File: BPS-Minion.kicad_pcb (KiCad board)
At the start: 2 copper layers, 85 x 66 mm, 128 parts, among them J1 TopConn, J10 TempConn2, J2 BottomConn, J3 DTENConfig, J4 IsoConfig, J5 IN, J6 OUT, J8 RegularSPIConn, J9 TempConn1, Q1 BSS308PE, Q10 BSS308PE, Q11 BSS308PE, Q12 BSS308PE, Q13 NSV1C201MZ4, Q2 BSS308PE, Q3 BSS308PE, Q4 BSS308PE, Q5 BSS308PE, Q6 BSS308PE, Q7 BSS308PE, Q8 BSS308PE, Q9 BSS308PE, SW1 Power Switch, U1 LTC6811-1, U2 HX1188FNL, U3 LTC6255, U4 LTC1380, U5 LTC1380

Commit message: Added measurements
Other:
- net class Default removed

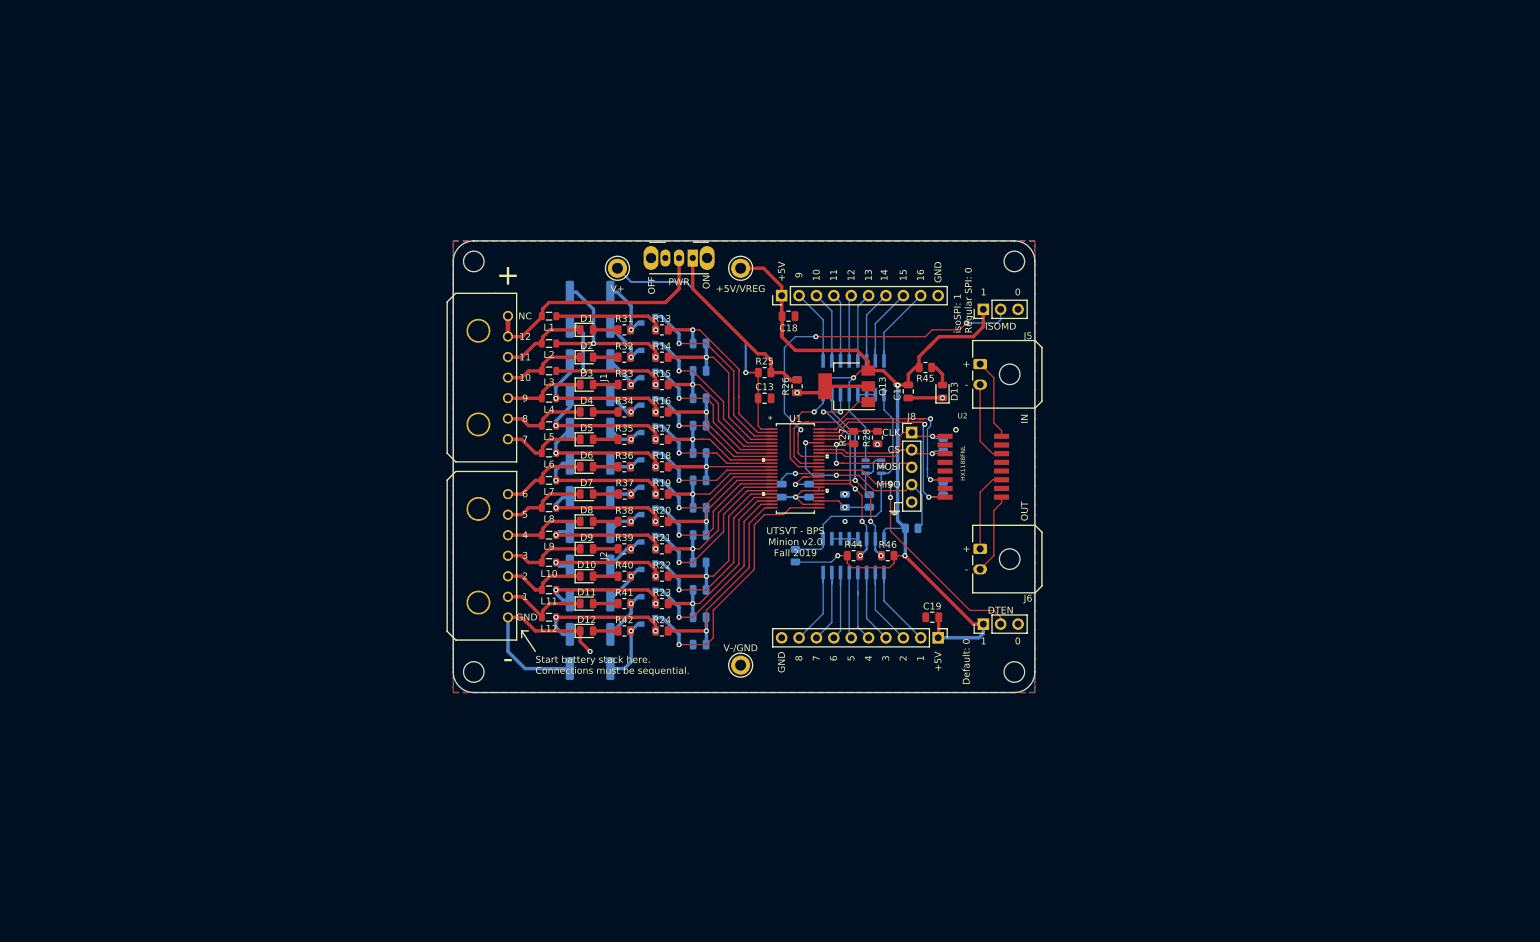
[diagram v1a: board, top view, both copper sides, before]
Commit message: define edge cuts for new volttemp
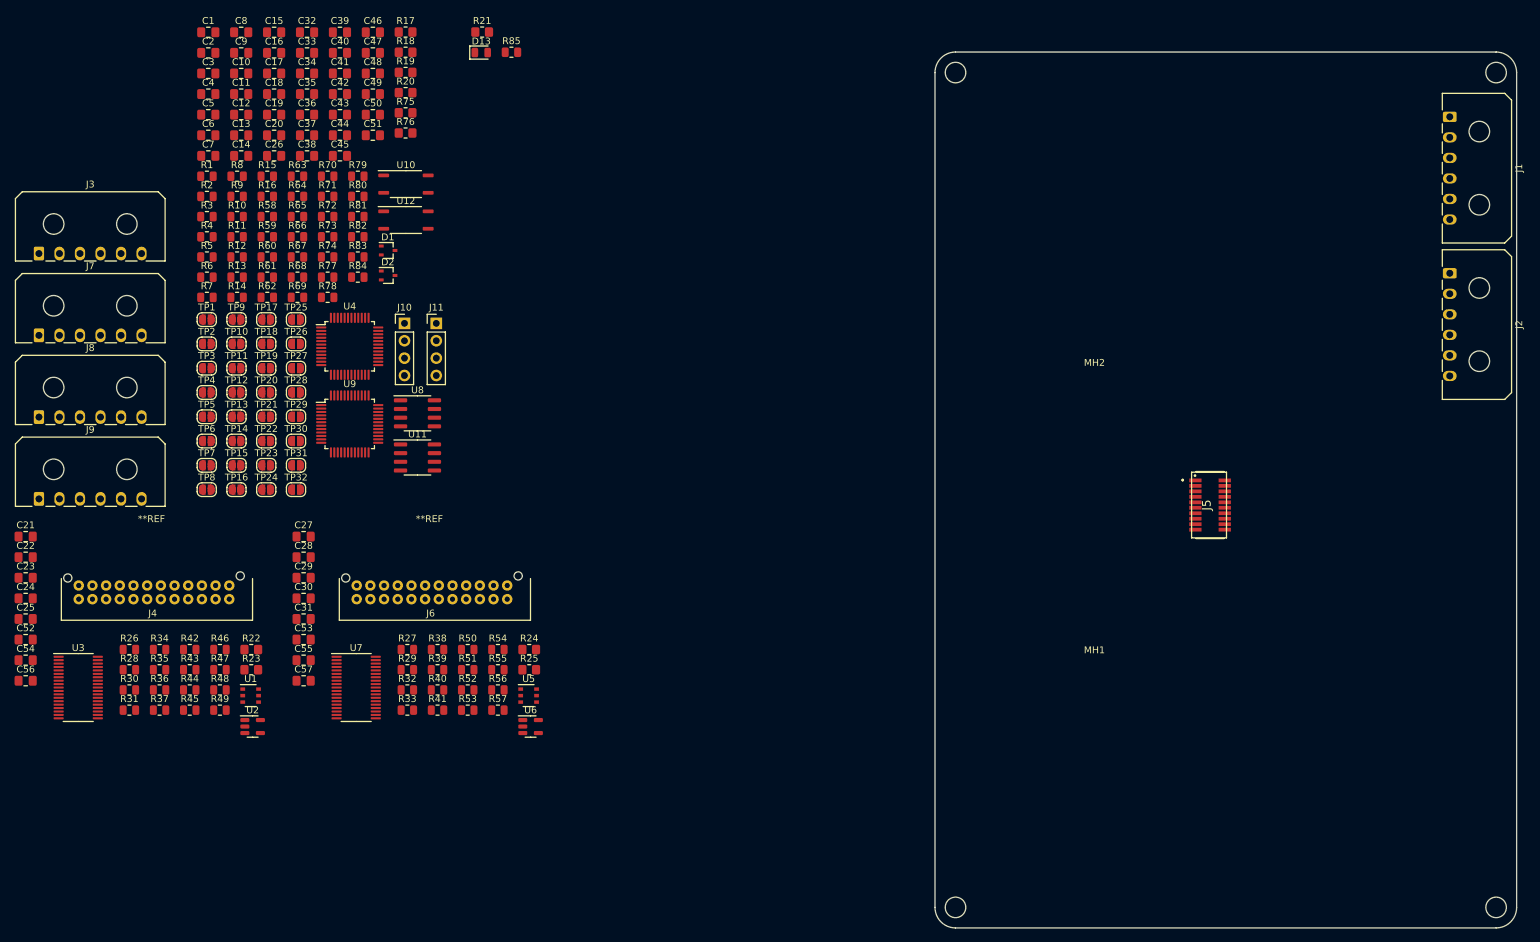
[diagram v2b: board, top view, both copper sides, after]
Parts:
- removed D10, D11, D12, D3, D4, D5, D6, D7, D8, D9: Red, LED_SMD:LED_0805_2012Metric
- removed L1, L10, L11, L12, L2, L3, L4, L5, L6, L7, L8, L9: 600, Inductor_SMD:L_0805_2012Metric
- removed Q1, Q10, Q11, Q12, Q2, Q3, Q4, Q5, Q6, Q7, Q8, Q9: BSS308PE, Package_TO_SOT_SMD:SOT-23
- removed Q13: NSV1C201MZ4, Package_TO_SOT_SMD:SOT-223
- removed SW1: Power Switch, Button_Switch_THT:SW_CuK_OS102011MA1QN1_SPDT_Angled
- added C21: 47n, Capacitor_SMD:C_0805_2012Metric_Pad1.18x1.45mm_HandSolder, F.Cu at (32.5, 93.2)
- added C22: 47n, Capacitor_SMD:C_0805_2012Metric_Pad1.18x1.45mm_HandSolder, F.Cu at (32.5, 96.2)
- added C23: 4.7u, Capacitor_SMD:C_0805_2012Metric_Pad1.18x1.45mm_HandSolder, F.Cu at (32.5, 99.2)
- added C24: 1u, Capacitor_SMD:C_0805_2012Metric_Pad1.18x1.45mm_HandSolder, F.Cu at (32.5, 102.2)
- added C25: 10u, Capacitor_SMD:C_0805_2012Metric_Pad1.18x1.45mm_HandSolder, F.Cu at (32.5, 105.2)
- added C26: 1u, Capacitor_SMD:C_0805_2012Metric_Pad1.18x1.45mm_HandSolder, F.Cu at (68.8, 37.6)
- added C27: 47n, Capacitor_SMD:C_0805_2012Metric_Pad1.18x1.45mm_HandSolder, F.Cu at (73.1, 93.2)
- added C28: 47n, Capacitor_SMD:C_0805_2012Metric_Pad1.18x1.45mm_HandSolder, F.Cu at (73.1, 96.2)
- added C29: 4.7u, Capacitor_SMD:C_0805_2012Metric_Pad1.18x1.45mm_HandSolder, F.Cu at (73.1, 99.2)
- added C30: 1u, Capacitor_SMD:C_0805_2012Metric_Pad1.18x1.45mm_HandSolder, F.Cu at (73.1, 102.2)
- added C31: 10u, Capacitor_SMD:C_0805_2012Metric_Pad1.18x1.45mm_HandSolder, F.Cu at (73.1, 105.2)
- added C32: 220nF, Capacitor_SMD:C_0805_2012Metric_Pad1.18x1.45mm_HandSolder, F.Cu at (73.6, 19.5)
- added C33: 220nF, Capacitor_SMD:C_0805_2012Metric_Pad1.18x1.45mm_HandSolder, F.Cu at (73.6, 22.5)
- added C34: 220nF, Capacitor_SMD:C_0805_2012Metric_Pad1.18x1.45mm_HandSolder, F.Cu at (73.6, 25.5)
- added C35: 220nF, Capacitor_SMD:C_0805_2012Metric_Pad1.18x1.45mm_HandSolder, F.Cu at (73.6, 28.5)
- added C36: 220nF, Capacitor_SMD:C_0805_2012Metric_Pad1.18x1.45mm_HandSolder, F.Cu at (73.6, 31.6)
- added C37: 220nF, Capacitor_SMD:C_0805_2012Metric_Pad1.18x1.45mm_HandSolder, F.Cu at (73.6, 34.6)
- added C38: 220nF, Capacitor_SMD:C_0805_2012Metric_Pad1.18x1.45mm_HandSolder, F.Cu at (73.6, 37.6)
- added C39: 220nF, Capacitor_SMD:C_0805_2012Metric_Pad1.18x1.45mm_HandSolder, F.Cu at (78.4, 19.5)
- added C40: 220nF, Capacitor_SMD:C_0805_2012Metric_Pad1.18x1.45mm_HandSolder, F.Cu at (78.4, 22.5)
- added C41: 220nF, Capacitor_SMD:C_0805_2012Metric_Pad1.18x1.45mm_HandSolder, F.Cu at (78.4, 25.5)
- added C42: 220nF, Capacitor_SMD:C_0805_2012Metric_Pad1.18x1.45mm_HandSolder, F.Cu at (78.4, 28.5)
- added C43: 220nF, Capacitor_SMD:C_0805_2012Metric_Pad1.18x1.45mm_HandSolder, F.Cu at (78.4, 31.6)
- added C44: 220nF, Capacitor_SMD:C_0805_2012Metric_Pad1.18x1.45mm_HandSolder, F.Cu at (78.4, 34.6)
- added C45: 220nF, Capacitor_SMD:C_0805_2012Metric_Pad1.18x1.45mm_HandSolder, F.Cu at (78.4, 37.6)
- added C46: 220nF, Capacitor_SMD:C_0805_2012Metric_Pad1.18x1.45mm_HandSolder, F.Cu at (83.3, 19.5)
- added C47: 220nF, Capacitor_SMD:C_0805_2012Metric_Pad1.18x1.45mm_HandSolder, F.Cu at (83.3, 22.5)
- added C48: .47u, Capacitor_SMD:C_0805_2012Metric_Pad1.18x1.45mm_HandSolder, F.Cu at (83.3, 25.5)
- added C49: 100p, Capacitor_SMD:C_0805_2012Metric_Pad1.18x1.45mm_HandSolder, F.Cu at (83.3, 28.5)
- added C50: 220nF, Capacitor_SMD:C_0805_2012Metric_Pad1.18x1.45mm_HandSolder, F.Cu at (83.3, 31.6)
- added C51: 1u, Capacitor_SMD:C_0805_2012Metric_Pad1.18x1.45mm_HandSolder, F.Cu at (83.3, 34.6)
- added C52: 1u, Capacitor_SMD:C_0805_2012Metric_Pad1.18x1.45mm_HandSolder, F.Cu at (32.5, 108.3)
- added C53: 1u, Capacitor_SMD:C_0805_2012Metric_Pad1.18x1.45mm_HandSolder, F.Cu at (73.1, 108.3)
- added C54: 1u, Capacitor_SMD:C_0805_2012Metric_Pad1.18x1.45mm_HandSolder, F.Cu at (32.5, 111.3)
- added C55: 1u, Capacitor_SMD:C_0805_2012Metric_Pad1.18x1.45mm_HandSolder, F.Cu at (73.1, 111.3)
- added C56: 1u, Capacitor_SMD:C_0805_2012Metric_Pad1.18x1.45mm_HandSolder, F.Cu at (32.5, 114.3)
- added C57: 1u, Capacitor_SMD:C_0805_2012Metric_Pad1.18x1.45mm_HandSolder, F.Cu at (73.1, 114.3)
- added J11: BMS2OTP, Connector_PinHeader_2.54mm:PinHeader_1x04_P2.54mm_Vertical, F.Cu at (92.5, 62.0)
- added J7: TopConn, Connector_Molex:Molex_Micro-Fit_3.0_43650-0600_1x06_P3.00mm_Horizontal, F.Cu at (34.5, 63.8)
- added R49: 10k, Resistor_SMD:R_0805_2012Metric, F.Cu at (60.9, 118.6)
- added R50: 10k, Resistor_SMD:R_0805_2012Metric, F.Cu at (97.1, 109.7)
- added R51: 10k, Resistor_SMD:R_0805_2012Metric, F.Cu at (97.1, 112.7)
- added R52: 10k, Resistor_SMD:R_0805_2012Metric, F.Cu at (97.1, 115.6)
- added R53: 10k, Resistor_SMD:R_0805_2012Metric, F.Cu at (97.1, 118.6)
- added R54: 10k, Resistor_SMD:R_0805_2012Metric, F.Cu at (101.5, 109.7)
- added R55: 10k, Resistor_SMD:R_0805_2012Metric, F.Cu at (101.5, 112.7)
- added R56: 10k, Resistor_SMD:R_0805_2012Metric, F.Cu at (101.5, 115.6)
- added R57: 10k, Resistor_SMD:R_0805_2012Metric, F.Cu at (101.5, 118.6)
- added R58: 20, Resistor_SMD:R_0805_2012Metric, F.Cu at (67.8, 46.5)
- added R59: 20, Resistor_SMD:R_0805_2012Metric, F.Cu at (67.8, 49.4)
- added R60: 20, Resistor_SMD:R_0805_2012Metric, F.Cu at (67.8, 52.4)
- added R61: 20, Resistor_SMD:R_0805_2012Metric, F.Cu at (67.8, 55.3)
- added R62: 20, Resistor_SMD:R_0805_2012Metric, F.Cu at (67.8, 58.2)
- added R63: 20, Resistor_SMD:R_0805_2012Metric, F.Cu at (72.2, 40.5)
- added R64: 20, Resistor_SMD:R_0805_2012Metric, F.Cu at (72.2, 43.5)
- added R65: 20, Resistor_SMD:R_0805_2012Metric, F.Cu at (72.2, 46.5)
- added R66: 20, Resistor_SMD:R_0805_2012Metric, F.Cu at (72.2, 49.4)
- added R67: 20, Resistor_SMD:R_0805_2012Metric, F.Cu at (72.2, 52.4)
- added R68: 20, Resistor_SMD:R_0805_2012Metric, F.Cu at (72.2, 55.3)
- added R69: 20, Resistor_SMD:R_0805_2012Metric, F.Cu at (72.2, 58.2)
- added R70: 20, Resistor_SMD:R_0805_2012Metric, F.Cu at (76.6, 40.5)
- added R71: 20, Resistor_SMD:R_0805_2012Metric, F.Cu at (76.6, 43.5)
- added R72: 20, Resistor_SMD:R_0805_2012Metric, F.Cu at (76.6, 46.5)
- added R73: 20, Resistor_SMD:R_0805_2012Metric, F.Cu at (76.6, 49.4)
- added R74: 20, Resistor_SMD:R_0805_2012Metric, F.Cu at (76.6, 52.4)
- added R75: 10k, Resistor_SMD:R_0805_2012Metric_Pad1.20x1.40mm_HandSolder, F.Cu at (88.0, 31.3)
- added R76: 100, Resistor_SMD:R_0805_2012Metric_Pad1.20x1.40mm_HandSolder, F.Cu at (88.0, 34.2)
- added R77: 10k, Resistor_SMD:R_0805_2012Metric, F.Cu at (76.6, 55.3)
- added R78: 10k, Resistor_SMD:R_0805_2012Metric, F.Cu at (76.6, 58.2)
- added R79: 220, Resistor_SMD:R_0805_2012Metric, F.Cu at (81.1, 40.5)
- added R80: 1k, Resistor_SMD:R_0805_2012Metric, F.Cu at (81.1, 43.5)
- added R81: 10k, Resistor_SMD:R_0805_2012Metric, F.Cu at (81.1, 46.5)
- added R82: 10k, Resistor_SMD:R_0805_2012Metric, F.Cu at (81.1, 49.4)
- added R83: 220, Resistor_SMD:R_0805_2012Metric, F.Cu at (81.1, 52.4)
- added R84: 10k, Resistor_SMD:R_0805_2012Metric, F.Cu at (81.1, 55.3)
- added R85: 50, Resistor_SMD:R_0805_2012Metric, F.Cu at (103.5, 22.4)
- added TP10: TestPoint_2Pole, Jumper:SolderJumper-2_P1.3mm_Open_RoundedPad1.0x1.5mm, F.Cu at (63.3, 65.0)
- added TP11: TestPoint_2Pole, Jumper:SolderJumper-2_P1.3mm_Open_RoundedPad1.0x1.5mm, F.Cu at (63.3, 68.6)
- added TP12: TestPoint_2Pole, Jumper:SolderJumper-2_P1.3mm_Open_RoundedPad1.0x1.5mm, F.Cu at (63.3, 72.2)
- added TP13: TestPoint_2Pole, Jumper:SolderJumper-2_P1.3mm_Open_RoundedPad1.0x1.5mm, F.Cu at (63.3, 75.7)
- added TP14: TestPoint_2Pole, Jumper:SolderJumper-2_P1.3mm_Open_RoundedPad1.0x1.5mm, F.Cu at (63.3, 79.2)
- added TP15: TestPoint_2Pole, Jumper:SolderJumper-2_P1.3mm_Open_RoundedPad1.0x1.5mm, F.Cu at (63.3, 82.8)
- added TP16: TestPoint_2Pole, Jumper:SolderJumper-2_P1.3mm_Open_RoundedPad1.0x1.5mm, F.Cu at (63.3, 86.3)
- added TP17: TestPoint_2Pole, Jumper:SolderJumper-2_P1.3mm_Open_RoundedPad1.0x1.5mm, F.Cu at (67.7, 61.5)
- added TP18: TestPoint_2Pole, Jumper:SolderJumper-2_P1.3mm_Open_RoundedPad1.0x1.5mm, F.Cu at (67.7, 65.0)
- added TP19: TestPoint_2Pole, Jumper:SolderJumper-2_P1.3mm_Open_RoundedPad1.0x1.5mm, F.Cu at (67.7, 68.6)
- added TP20: TestPoint_2Pole, Jumper:SolderJumper-2_P1.3mm_Open_RoundedPad1.0x1.5mm, F.Cu at (67.7, 72.2)
- added TP21: TestPoint_2Pole, Jumper:SolderJumper-2_P1.3mm_Open_RoundedPad1.0x1.5mm, F.Cu at (67.7, 75.7)
- added TP22: TestPoint_2Pole, Jumper:SolderJumper-2_P1.3mm_Open_RoundedPad1.0x1.5mm, F.Cu at (67.7, 79.2)
- added TP23: TestPoint_2Pole, Jumper:SolderJumper-2_P1.3mm_Open_RoundedPad1.0x1.5mm, F.Cu at (67.7, 82.8)
- added TP24: TestPoint_2Pole, Jumper:SolderJumper-2_P1.3mm_Open_RoundedPad1.0x1.5mm, F.Cu at (67.7, 86.3)
- added TP25: TestPoint_2Pole, Jumper:SolderJumper-2_P1.3mm_Open_RoundedPad1.0x1.5mm, F.Cu at (72.0, 61.5)
- added TP26: TestPoint_2Pole, Jumper:SolderJumper-2_P1.3mm_Open_RoundedPad1.0x1.5mm, F.Cu at (72.0, 65.0)
- added TP27: TestPoint_2Pole, Jumper:SolderJumper-2_P1.3mm_Open_RoundedPad1.0x1.5mm, F.Cu at (72.0, 68.6)
- added TP28: TestPoint_2Pole, Jumper:SolderJumper-2_P1.3mm_Open_RoundedPad1.0x1.5mm, F.Cu at (72.0, 72.2)
- added TP29: TestPoint_2Pole, Jumper:SolderJumper-2_P1.3mm_Open_RoundedPad1.0x1.5mm, F.Cu at (72.0, 75.7)
- added TP30: TestPoint_2Pole, Jumper:SolderJumper-2_P1.3mm_Open_RoundedPad1.0x1.5mm, F.Cu at (72.0, 79.2)
- added TP31: TestPoint_2Pole, Jumper:SolderJumper-2_P1.3mm_Open_RoundedPad1.0x1.5mm, F.Cu at (72.0, 82.8)
- added TP32: TestPoint_2Pole, Jumper:SolderJumper-2_P1.3mm_Open_RoundedPad1.0x1.5mm, F.Cu at (72.0, 86.3)
- added TP4: TestPoint_2Pole, Jumper:SolderJumper-2_P1.3mm_Open_RoundedPad1.0x1.5mm, F.Cu at (59.0, 72.2)
- added TP5: TestPoint_2Pole, Jumper:SolderJumper-2_P1.3mm_Open_RoundedPad1.0x1.5mm, F.Cu at (59.0, 75.7)
- added TP6: TestPoint_2Pole, Jumper:SolderJumper-2_P1.3mm_Open_RoundedPad1.0x1.5mm, F.Cu at (59.0, 79.2)
- added TP7: TestPoint_2Pole, Jumper:SolderJumper-2_P1.3mm_Open_RoundedPad1.0x1.5mm, F.Cu at (59.0, 82.8)
- added TP8: TestPoint_2Pole, Jumper:SolderJumper-2_P1.3mm_Open_RoundedPad1.0x1.5mm, F.Cu at (59.0, 86.3)
- added TP9: TestPoint_2Pole, Jumper:SolderJumper-2_P1.3mm_Open_RoundedPad1.0x1.5mm, F.Cu at (63.3, 61.5)
- added U10: TLP185, Package_SO:SOIC-4_4.55x3.7mm_P2.54mm, F.Cu at (88.1, 41.7)
- added U11: ISO1640BDR, Package_SO:SOIC-8_3.9x4.9mm_P1.27mm, F.Cu at (89.8, 81.7)
- added U12: TLP185, Package_SO:SOIC-4_4.55x3.7mm_P2.54mm, F.Cu at (88.1, 47.0)
- added U6: LM321, Package_TO_SOT_SMD:SOT-23-5, F.Cu at (106.3, 121.0)
- added U7: ADS7953SBDBT, Package_SO:TSSOP-38_4.4x9.7mm_P0.5mm, F.Cu at (80.8, 115.3)
- added U8: ISO1640BDR, Package_SO:SOIC-8_3.9x4.9mm_P1.27mm, F.Cu at (89.8, 75.2)
- added U9: BQ7695201PFBR, Package_QFP:TQFP-48_7x7mm_P0.5mm, F.Cu at (79.9, 76.8)
- C1, C10, C11, C12, C2, C3, C4, C5, C6, C7, C8, C9: value 10n -> 220nF; footprint Capacitor_SMD:C_0805_2012Metric -> Capacitor_SMD:C_0805_2012Metric_Pad1.18x1.45mm_HandSolder; moved to F.Cu
- C13: value 100n -> 220nF; footprint Capacitor_SMD:C_0805_2012Metric -> Capacitor_SMD:C_0805_2012Metric_Pad1.18x1.45mm_HandSolder
- C14, C15: value 1u -> 220nF; footprint Capacitor_SMD:C_0805_2012Metric -> Capacitor_SMD:C_0805_2012Metric_Pad1.18x1.45mm_HandSolder; moved to F.Cu
- C16: value 1u -> 220nF; footprint Capacitor_SMD:C_0805_2012Metric -> Capacitor_SMD:C_0805_2012Metric_Pad1.18x1.45mm_HandSolder
- C17: value 10n -> 4.7u; footprint Capacitor_SMD:C_0805_2012Metric -> Capacitor_SMD:C_0805_2012Metric_Pad1.18x1.45mm_HandSolder; moved to F.Cu
- C18: value 100n -> 4.7u; footprint Capacitor_SMD:C_0805_2012Metric -> Capacitor_SMD:C_0805_2012Metric_Pad1.18x1.45mm_HandSolder
- C19: value 100n -> .47u; footprint Capacitor_SMD:C_0805_2012Metric -> Capacitor_SMD:C_0805_2012Metric_Pad1.18x1.45mm_HandSolder
- C20: value 100n -> 100p; footprint Capacitor_SMD:C_0805_2012Metric -> Capacitor_SMD:C_0805_2012Metric_Pad1.18x1.45mm_HandSolder; moved to F.Cu
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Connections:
- C1 pad 1: GND -> Net-(J3-Pin_6)
- C1 pad 2: Net-(C1-Pad2) -> GND2
- C10 pad 1: Net-(C10-Pad1) -> Net-(J8-Pin_3)
- C10 pad 2: Net-(C10-Pad2) -> Net-(J8-Pin_2)
- C11 pad 1: Net-(C10-Pad2) -> Net-(J8-Pin_4)
- C11 pad 2: Net-(C11-Pad2) -> Net-(J8-Pin_3)
- C12 pad 1: Net-(C11-Pad2) -> Net-(J8-Pin_5)
- C12 pad 2: Net-(C12-Pad2) -> Net-(J8-Pin_4)
- C13 pad 1: Net-(C13-Pad1) -> Net-(J8-Pin_6)
- C13 pad 2: GND -> Net-(J8-Pin_5)
- C14 pad 1: Net-(C14-Pad1) -> Net-(J9-Pin_1)
- C14 pad 2: GND -> Net-(J8-Pin_6)
- C15 pad 1: Net-(C15-Pad1) -> Net-(J9-Pin_2)
- C15 pad 2: GND -> Net-(J9-Pin_1)
- C16 pad 1: +5V -> /BMS/PACK+
- C16 pad 2: GND -> Net-(J9-Pin_2)
- C17 pad 1: GND -> GND2
- C17 pad 2: /GPIO1 -> Net-(U9-REG18)
- C18 pad 1: +5V -> GND1
- C18 pad 2: GND -> Net-(U4-REG18)
- C19 pad 1: +5V -> Net-(U4-CP1)
- C19 pad 2: GND -> /BMS/BMS1BAT
- C2 pad 1: Net-(C1-Pad2) -> Net-(J7-Pin_1)
- C2 pad 2: Net-(C2-Pad2) -> Net-(J3-Pin_6)
- C20 pad 1: Net-(C20-Pad1) -> GND1
- C20 pad 2: GND -> /BMS/BMS1BAT
- C3 pad 1: Net-(C2-Pad2) -> Net-(J7-Pin_2)
- C3 pad 2: Net-(C3-Pad2) -> Net-(J7-Pin_1)
- C4 pad 1: Net-(C3-Pad2) -> Net-(J7-Pin_3)
- C4 pad 2: Net-(C4-Pad2) -> Net-(J7-Pin_2)
- C5 pad 1: Net-(C4-Pad2) -> Net-(J7-Pin_4)
- C5 pad 2: Net-(C5-Pad2) -> Net-(J7-Pin_3)
- C6 pad 1: Net-(C5-Pad2) -> Net-(J7-Pin_5)
- C6 pad 2: Net-(C6-Pad2) -> Net-(J7-Pin_4)
- C7 pad 1: Net-(C6-Pad2) -> Net-(J7-Pin_6)
- C7 pad 2: Net-(C7-Pad2) -> Net-(J7-Pin_5)
- C8 pad 1: Net-(C7-Pad2) -> Net-(J8-Pin_1)
- C8 pad 2: Net-(C8-Pad2) -> Net-(J7-Pin_6)
- C9 pad 1: Net-(C8-Pad2) -> Net-(J8-Pin_2)
- C9 pad 2: Net-(C10-Pad1) -> Net-(J8-Pin_1)
- D1 pad 1: /Batt11 -> GND2
- D1 pad 2: Net-(D1-Pad2) -> unconnected-(D1-NC-Pad2)
- D13 pad 2: Net-(D13-Pad2) -> Net-(D13-A)
- D2 pad 1: /Batt10 -> /BMS/PACK+
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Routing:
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- removed copper zone on B.Cu, net GND
- removed copper zone on F.Cu, net GND
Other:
- board size 85 x 66 mm -> 85 x 128 mm
- board text added: "MH1"
- board text added: "MH2"
- board text added: "Peripheral SOM"
- board text removed: "+"
- board text removed: "+5V"
- board text removed: "+5V/VREG"
- board text removed: "-"
- board text removed: "0"
- board text removed: "1"
- board text removed: "10"
- board text removed: "11"
- board text removed: "12"
- board text removed: "13"
- board text removed: "14"
- board text removed: "15"
- board text removed: "16"
- board text removed: "2"
- board text removed: "3"
- board text removed: "4"
- board text removed: "5"
- board text removed: "6"
- board text removed: "7"
- board text removed: "8"
- board text removed: "9"
- board text removed: ":)"
- board text removed: "CLK"
- board text removed: "CS"
- board text removed: "DTEN"
- board text removed: "Default: 0"
- board text removed: "Dr. Gary Hallock"
- board text removed: "GND"
- board text removed: "IN"
- board text removed: "ISOMD"
- board text removed: "MISO"
- board text removed: "MOSI"
- board text removed: "NC"
- board text removed: "OFF"
- board text removed: "ON"
- board text removed: "OUT"
- board text removed: "PWR"
- board text removed: "Start battery stack here. Connections must be sequential."
- board text removed: "UTSVT - BPS Minion v2.0 Fall 2019"
- board text removed: "Unused pins must be shorted. C1 to the number of modules must have caps. All other caps must be replaced with 0 Ohm resistors. E.g. if only 8 modules are connected, C9-12 should be replaced with 0 Ohm Resistor while C1-8 are preserved."
- board text removed: "V+"
- board text removed: "V-/GND"
- board text removed: "isoSPI: 1 Regular SPI: 0"

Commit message: battery pack draft design
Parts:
- C32, C34, C36, J2, R58, R59, R60, R61, R62: moved to B.Cu
- moved J2 354.5 mm to (-83.1, -89.8)
- moved R63 213.6 mm to (-105.9, -77.3)
- moved R64 213.6 mm to (-105.9, -74.3)
- moved R65 213.6 mm to (-105.9, -71.4)
- moved R66 213.6 mm to (-105.9, -68.4)
- moved R67 213.6 mm to (-105.9, -65.5)
- moved R68 213.6 mm to (-105.9, -62.5)
- moved R69 213.6 mm to (-105.9, -59.6)
- moved TP21 213.6 mm to (-110.5, -42.1)
- moved TP22 213.6 mm to (-110.5, -38.6)
- moved TP23 213.6 mm to (-110.5, -35.0)
- moved C37 213.6 mm to (-104.5, -83.3)
- moved C38 213.6 mm to (-104.5, -80.3)
- moved C39 213.6 mm to (-99.7, -98.3)
- moved C40 213.6 mm to (-99.7, -95.3)
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
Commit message: battery pack draft design
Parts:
- C37, C39, C41: moved to B.Cu
- J2, R58, R59, R60, R61, R62: moved to F.Cu
- moved C39 375.2 mm to (238.9, 63.3), turned to 90 degrees
- moved C40 374.7 mm to (238.9, 65.3), turned to 90 degrees
- moved C41 374.3 mm to (238.9, 67.3), turned to 90 degrees
- moved C42 373.9 mm to (238.9, 69.3), turned to 90 degrees
- moved C37 371.8 mm to (238.9, 59.2), turned to 90 degrees
- moved C38 371.4 mm to (238.9, 61.2), turned to 90 degrees
- moved R64 367.1 mm to (236.1, 59.2)
- moved R65 366.8 mm to (236.1, 61.2)
- moved R66 366.5 mm to (236.1, 63.2)
- moved R67 366.1 mm to (236.1, 65.3)
- moved R68 365.8 mm to (236.1, 67.3)
- moved R69 365.5 mm to (236.1, 69.3)
- moved TP25 361.1 mm to (233.1, 67.3), turned to -90 degrees
- moved TP26 360.9 mm to (233.1, 70.3), turned to -90 degrees
- moved TP22 357.0 mm to (233.1, 58.2), turned to -90 degrees
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
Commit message: battery pack half done
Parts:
- C1, C3, C44, C46, C5, C7: moved to B.Cu
- moved J3 208.8 mm to (241.4, 79.4), turned to -90 degrees
- moved C1 193.8 mm to (238.9, 92.0), turned to 90 degrees
- moved R1 184.4 mm to (236.1, 91.9), turned to 180 degrees
- moved C2 183.1 mm to (225.6, 99.1), turned to 90 degrees
- moved TP1 177.0 mm to (233.1, 93.1), turned to -90 degrees
- moved C46 170.0 mm to (238.9, 88.0), turned to 90 degrees
- moved C47 169.6 mm to (238.9, 90.0), turned to 90 degrees
- moved C43 168.0 mm to (238.8, 81.7), turned to 90 degrees
- moved C44 167.8 mm to (238.8, 83.8), turned to 90 degrees
- moved C45 167.5 mm to (238.8, 86.0), turned to 90 degrees
- moved R70 164.7 mm to (236.1, 81.8), turned to 180 degrees
- moved R71 164.4 mm to (236.1, 83.8), turned to 180 degrees
- moved R72 164.2 mm to (236.1, 85.8), turned to 180 degrees
- moved R73 164.0 mm to (236.1, 87.9), turned to 180 degrees
- moved R74 163.8 mm to (236.1, 89.9), turned to 180 degrees
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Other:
- board size 85 x 128 mm -> 85 x 169.8 mm

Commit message: why so many bugs >:(
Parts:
- removed the C11 at (64.0, 28.5)
- removed the C12 at (64.0, 31.6)
- removed the C13 at (64.0, 34.6)
- removed the C15 at (68.8, 19.5)
- removed the C16 at (68.8, 22.5)
- removed the C3 at (49.8, -61.3)
- removed the C4 at (49.8, -59.2)
- removed the C5 at (49.8, -57.2)
- removed the C6 at (49.8, -55.1)
- removed the C8 at (64.0, 19.5)
- removed the C9 at (64.0, 22.5)
- removed the J1 at (241.4, 34.1)
- removed the J2 at (241.4, 56.8)
- removed the J3 at (241.4, 79.4)
- removed the R1 at (236.1, 91.9)
- removed the R10 at (63.4, 46.5)
- removed the R11 at (63.4, 49.4)
- removed the R12 at (63.4, 52.4)
- removed the R13 at (63.4, 55.3)
- removed the R14 at (63.4, 58.2)
- removed the R15 at (67.8, 40.5)
- removed the R16 at (67.8, 43.5)
- removed the R2 at (32.0, -44.5)
- removed the R3 at (32.0, -41.6)
- removed the R4 at (32.0, -38.6)
- removed the R5 at (32.0, -35.7)
- removed the R6 at (32.0, -32.7)
- removed the R7 at (32.0, -29.8)
- removed the R8 at (63.4, 40.5)
- removed the R9 at (63.4, 43.5)
- removed the U10 at (88.1, 41.7)
- added C25: 220nF, Capacitor_SMD:C_0805_2012Metric_Pad1.18x1.45mm_HandSolder, F.Cu at (231.9, 33.5)
- added C26: 220nF, Capacitor_SMD:C_0805_2012Metric_Pad1.18x1.45mm_HandSolder, F.Cu at (228.3, 35.8)
- added C27: 220nF, Capacitor_SMD:C_0805_2012Metric_Pad1.18x1.45mm_HandSolder, F.Cu at (231.9, 38.1)
- added C28: 220nF, Capacitor_SMD:C_0805_2012Metric_Pad1.18x1.45mm_HandSolder, F.Cu at (228.3, 40.4)
- added C29: 220nF, Capacitor_SMD:C_0805_2012Metric_Pad1.18x1.45mm_HandSolder, F.Cu at (231.9, 42.7)
- added C3: 1u, Capacitor_SMD:C_0805_2012Metric_Pad1.18x1.45mm_HandSolder, F.Cu at (78.7, 114.2)
- added C3: 10u, Capacitor_SMD:C_0805_2012Metric_Pad1.18x1.45mm_HandSolder, F.Cu at (89.0, 144.7)
- added C30: 220nF, Capacitor_SMD:C_0805_2012Metric_Pad1.18x1.45mm_HandSolder, F.Cu at (228.3, 45.0)
- added C31: 220nF, Capacitor_SMD:C_0805_2012Metric_Pad1.18x1.45mm_HandSolder, F.Cu at (152.5, -75.7)
- added C48: 220nF, Capacitor_SMD:C_0805_2012Metric_Pad1.18x1.45mm_HandSolder, F.Cu at (126.8, -25.4)
- added C49: 220nF, Capacitor_SMD:C_0805_2012Metric_Pad1.18x1.45mm_HandSolder, F.Cu at (101.1, -40.4)
- added C51: 220nF, Capacitor_SMD:C_0805_2012Metric_Pad1.18x1.45mm_HandSolder, F.Cu at (101.1, -34.4)
- added C52: 220nF, Capacitor_SMD:C_0805_2012Metric_Pad1.18x1.45mm_HandSolder, F.Cu at (101.1, -31.4)
- added C53: 220nF, Capacitor_SMD:C_0805_2012Metric_Pad1.18x1.45mm_HandSolder, F.Cu at (101.1, -28.4)
- added C54: 220nF, Capacitor_SMD:C_0805_2012Metric_Pad1.18x1.45mm_HandSolder, F.Cu at (101.1, -25.4)
- added C55: 220nF, Capacitor_SMD:C_0805_2012Metric_Pad1.18x1.45mm_HandSolder, F.Cu at (126.8, -75.7)
- added C56: 220nF, Capacitor_SMD:C_0805_2012Metric_Pad1.18x1.45mm_HandSolder, F.Cu at (126.8, -72.7)
- added C57: 220nF, Capacitor_SMD:C_0805_2012Metric_Pad1.18x1.45mm_HandSolder, F.Cu at (126.8, -69.7)
- added C58: 220nF, Capacitor_SMD:C_0805_2012Metric_Pad1.18x1.45mm_HandSolder, F.Cu at (126.8, -66.7)
- added C59: 220nF, Capacitor_SMD:C_0805_2012Metric_Pad1.18x1.45mm_HandSolder, F.Cu at (126.8, -63.6)
- added C60: 220nF, Capacitor_SMD:C_0805_2012Metric_Pad1.18x1.45mm_HandSolder, F.Cu at (126.8, -60.6)
- added D2: 1N4448W, Diode_SMD:D_SOD-123, F.Cu at (58.6, 62.9)
- added D3: 1N4448W, Diode_SMD:D_SOD-123, F.Cu at (58.6, 66.2)
- added J10: TopConn, Connector_Molex:Molex_Micro-Fit_3.0_43650-0600_1x06_P3.00mm_Horizontal, F.Cu at (98.7, -43.9)
- added J11: TopConn, Connector_Molex:Molex_Micro-Fit_3.0_43650-0600_1x06_P3.00mm_Horizontal, F.Cu at (124.4, -79.2)
- added J6: TopConn, Connector_Molex:Molex_Micro-Fit_3.0_43650-0600_1x06_P3.00mm_Horizontal, F.Cu at (240.9, 32.6)
- added R53: 20, Resistor_SMD:R_0805_2012Metric, F.Cu at (234.9, 34.8)
- added R54: 20, Resistor_SMD:R_0805_2012Metric, F.Cu at (234.9, 37.1)
- added R55: 20, Resistor_SMD:R_0805_2012Metric, F.Cu at (234.9, 39.4)
- added R56: 20, Resistor_SMD:R_0805_2012Metric, F.Cu at (234.9, 41.7)
- added R57: 20, Resistor_SMD:R_0805_2012Metric, F.Cu at (234.9, 43.9)
- added R75: 20, Resistor_SMD:R_0805_2012Metric, F.Cu at (131.4, -28.7)
- added R76: 20, Resistor_SMD:R_0805_2012Metric, F.Cu at (131.4, -25.7)
- added R77: 20, Resistor_SMD:R_0805_2012Metric, F.Cu at (105.7, -40.5)
- added R78: 20, Resistor_SMD:R_0805_2012Metric, F.Cu at (105.7, -37.5)
- added R79: 20, Resistor_SMD:R_0805_2012Metric, F.Cu at (105.7, -34.6)
- added R80: 20, Resistor_SMD:R_0805_2012Metric, F.Cu at (105.7, -31.6)
- added R81: 20, Resistor_SMD:R_0805_2012Metric, F.Cu at (105.7, -28.7)
- added R82: 20, Resistor_SMD:R_0805_2012Metric, F.Cu at (105.7, -25.7)
- added R83: 20, Resistor_SMD:R_0805_2012Metric, F.Cu at (131.4, -75.7)
- added R84: 20, Resistor_SMD:R_0805_2012Metric, F.Cu at (131.4, -72.8)
- added R85: 20, Resistor_SMD:R_0805_2012Metric, F.Cu at (131.4, -69.8)
- added R86: 20, Resistor_SMD:R_0805_2012Metric, F.Cu at (131.4, -66.9)
- added R87: 20, Resistor_SMD:R_0805_2012Metric, F.Cu at (131.4, -63.9)
- added R88: 20, Resistor_SMD:R_0805_2012Metric, F.Cu at (131.4, -61.0)
- added TP33: TestPoint_2Pole, Jumper:SolderJumper-2_P1.3mm_Open_RoundedPad1.0x1.5mm, F.Cu at (122.2, -68.3)
- added TP34: TestPoint_2Pole, Jumper:SolderJumper-2_P1.3mm_Open_RoundedPad1.0x1.5mm, F.Cu at (122.2, -64.8)
- added TP35: TestPoint_2Pole, Jumper:SolderJumper-2_P1.3mm_Open_RoundedPad1.0x1.5mm, F.Cu at (122.2, -61.2)
- added TP36: TestPoint_2Pole, Jumper:SolderJumper-2_P1.3mm_Open_RoundedPad1.0x1.5mm, F.Cu at (122.2, -57.7)
- added U1: REF35250QDBVR, Package_SO:TSOP-6_1.65x3.05mm_P0.95mm, F.Cu at (83.1, 144.8)
- added U4: EL3H7, Package_SO:SOP-4_4.4x2.6mm_P1.27mm, F.Cu at (39.3, 37.6)
- added U7: EL3H7, Package_SO:SOP-4_4.4x2.6mm_P1.27mm, F.Cu at (84.8, 45.5)
- C1: value 220nF -> 10u; moved to F.Cu
- C10, C14, C2: value 220nF -> 1u
- C32, C34, C36, C37, C39, C41, C44, C46: moved to F.Cu
- C7: value 220nF -> 1u; moved to F.Cu
- U12: value TLP185 -> MIC5317-2.5xM5; footprint Package_SO:SOIC-4_4.55x3.7mm_P2.54mm -> Package_TO_SOT_SMD:SOT-23-5
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- renumbered C48 to C11, C49 to C12, C23 to C12, C24 to C13, C51 to C13, C25 to C14, C56 to C15, C21 to C16, C22 to C17, C52 to C18, C54 to C19, C29 to C20, C57 to C20, C30 to C21, C27 to C21, C31 to C22, C28 to C22, C53 to C23, C55 to C24, C18 to C4, C19 to C5, C20 to C6, C26 to C8, C17 to C9, D13 to D1, D1 to D2, D2 to D3, J5 to J1, J10 to J2, J11 to J3, J6 to J5, R21 to R1, R79 to R10, R17 to R11, R75 to R12, R80 to R13, R77 to R14, R78 to R15, R76 to R16, R26 to R17, R42 to R18, R28 to R19, R85 to R2, R43 to R20, R30 to R21, R44 to R22, R31 to R23, R45 to R24, R34 to R25, R46 to R26, R35 to R27, R47 to R28, R36 to R29, R83 to R3, R48 to R30, R37 to R31, R49 to R32, R22 to R33, R23 to R34, R27 to R35, R50 to R36, R29 to R37, R51 to R38, R32 to R39, R81 to R4, R52 to R40, R33 to R41, R53 to R42, R38 to R43, R54 to R44, R39 to R45, R55 to R46, R40 to R47, R56 to R48, R41 to R49, R18 to R5, R57 to R50, R24 to R51, R25 to R52, R19 to R6, R82 to R7, R84 to R8, R20 to R9, U5 to U10, U6 to U10, U7 to U11, U4 to U2, U11 to U3, U9 to U5, U8 to U6, U1 to U7, U2 to U8, U3 to U9
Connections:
- C1 pad 1: Net-(J3-Pin_6) -> GNDA
- C1 pad 2: GND2 -> VDDA
- C10 pad 1: Net-(J8-Pin_3) -> GND
- C10 pad 2: Net-(J8-Pin_2) -> +3.3V
- C14 pad 1: Net-(J9-Pin_1) -> /BMS/BMS2Reg1
- C14 pad 2: Net-(J8-Pin_6) -> GND2
- C2 pad 1: Net-(J7-Pin_1) -> +2V5
- C2 pad 2: Net-(J3-Pin_6) -> GNDA
- C32 pad 1: Net-(J1-Pin_2) -> /BMS/cell7
- C32 pad 2: Net-(J1-Pin_1) -> /BMS/cell6
- C33 pad 1: Net-(J1-Pin_3) -> /BMS/cell8
- C33 pad 2: Net-(J1-Pin_2) -> /BMS/cell7
- C34 pad 1: Net-(J1-Pin_4) -> /BMS/cell9
- C34 pad 2: Net-(J1-Pin_3) -> /BMS/cell8
- C35 pad 1: Net-(J1-Pin_5) -> /BMS/cell10
- C35 pad 2: Net-(J1-Pin_4) -> /BMS/cell9
- C36 pad 1: Net-(J1-Pin_6) -> /BMS/cell11
- C36 pad 2: Net-(J1-Pin_5) -> /BMS/cell10
- C37 pad 1: Net-(J2-Pin_1) -> /BMS/cell12
- C37 pad 2: Net-(J1-Pin_6) -> /BMS/cell11
- C38 pad 1: Net-(J2-Pin_2) -> /BMS/cell13
- C38 pad 2: Net-(J2-Pin_1) -> /BMS/cell12
- C39 pad 1: Net-(J2-Pin_3) -> /BMS/cell14
- C39 pad 2: Net-(J2-Pin_2) -> /BMS/cell13
- C40 pad 1: Net-(J2-Pin_4) -> /BMS/cell15
- C40 pad 2: Net-(J2-Pin_3) -> /BMS/cell14
- C41 pad 1: Net-(J2-Pin_5) -> GND2
- C41 pad 2: Net-(J2-Pin_4) -> /BMS/cell15
- C42 pad 1: Net-(J2-Pin_6) -> /BMS/cell17
- C42 pad 2: Net-(J2-Pin_5) -> GND2
- C43 pad 1: Net-(J3-Pin_1) -> /BMS/cell18
- C43 pad 2: Net-(J2-Pin_6) -> /BMS/cell17
- C44 pad 1: Net-(J3-Pin_2) -> /BMS/cell19
- C44 pad 2: Net-(J3-Pin_1) -> /BMS/cell18
- C45 pad 1: Net-(J3-Pin_3) -> /BMS/cell20
- C45 pad 2: Net-(J3-Pin_2) -> /BMS/cell19
- C46 pad 1: Net-(J3-Pin_4) -> /BMS/cell21
- C46 pad 2: Net-(J3-Pin_3) -> /BMS/cell20
- C47 pad 1: GND2 -> /BMS/cell22
- C47 pad 2: Net-(J3-Pin_4) -> /BMS/cell21
- C50 pad 1: Net-(J1-Pin_1) -> /BMS/cell25
- C50 pad 2: GND1 -> /BMS/cell24
- C7 pad 1: Net-(J7-Pin_6) -> /BMS/BMS1Reg1
- C7 pad 2: Net-(J7-Pin_5) -> GND1
- J9 pad 3: /BMS/PACK+ -> Net-(J9-Pin_3)
- J9 pad 4: unconnected-(J9-Pin_4-Pad4) -> Net-(J9-Pin_4)
- J9 pad 5: unconnected-(J9-Pin_5-Pad5) -> Net-(J9-Pin_5)
- J9 pad 6: unconnected-(J9-Pin_6-Pad6) -> Net-(J9-Pin_6)
- R10 pad 2: Net-(R79-Pad2) -> Net-(R10-Pad2)
- R17 pad 2: /Temperature/2V5_Ref -> +2V5
- R18 pad 2: /Temperature/2V5_Ref -> +2V5
- R19 pad 2: /Temperature/2V5_Ref -> +2V5
- R20 pad 2: /Temperature/2V5_Ref -> +2V5
- R21 pad 2: /Temperature/2V5_Ref -> +2V5
- R22 pad 2: /Temperature/2V5_Ref -> +2V5
- R23 pad 2: /Temperature/2V5_Ref -> +2V5
- R24 pad 2: /Temperature/2V5_Ref -> +2V5
- R25 pad 2: /Temperature/2V5_Ref -> +2V5
- R26 pad 2: /Temperature/2V5_Ref -> +2V5
- R27 pad 2: /Temperature/2V5_Ref -> +2V5
- R28 pad 2: /Temperature/2V5_Ref -> +2V5
- R29 pad 2: /Temperature/2V5_Ref -> +2V5
- R30 pad 2: /Temperature/2V5_Ref -> +2V5
- R31 pad 2: /Temperature/2V5_Ref -> +2V5
- R32 pad 2: /Temperature/2V5_Ref -> +2V5
- R35 pad 2: /Temperature1/2V5_Ref -> +2V5
- R36 pad 2: /Temperature1/2V5_Ref -> +2V5
- R37 pad 2: /Temperature1/2V5_Ref -> +2V5
- R38 pad 2: /Temperature1/2V5_Ref -> +2V5
- R39 pad 2: /Temperature1/2V5_Ref -> +2V5
- R40 pad 2: /Temperature1/2V5_Ref -> +2V5
- R41 pad 2: /Temperature1/2V5_Ref -> +2V5
- R42 pad 2: /Temperature1/2V5_Ref -> +2V5
- R43 pad 2: /Temperature1/2V5_Ref -> +2V5
- R44 pad 2: /Temperature1/2V5_Ref -> +2V5
- R45 pad 2: /Temperature1/2V5_Ref -> +2V5
- R46 pad 2: /Temperature1/2V5_Ref -> +2V5
- R47 pad 2: /Temperature1/2V5_Ref -> +2V5
- R48 pad 2: /Temperature1/2V5_Ref -> +2V5
- R49 pad 2: /Temperature1/2V5_Ref -> +2V5
- R50 pad 2: /Temperature1/2V5_Ref -> +2V5
- R58 pad 1: Net-(J1-Pin_1) -> Net-(J6-Pin_6)
- R58 pad 2: /BMS/cell0 -> /BMS/cell5
- R59 pad 1: Net-(J1-Pin_2) -> Net-(J7-Pin_1)
- R59 pad 2: /BMS/cell1 -> /BMS/cell6
- R60 pad 1: Net-(J1-Pin_3) -> Net-(J7-Pin_2)
- R60 pad 2: /BMS/cell2 -> /BMS/cell7
- R61 pad 1: Net-(J1-Pin_4) -> Net-(J7-Pin_3)
- R61 pad 2: /BMS/cell3 -> /BMS/cell8
- R62 pad 1: Net-(J1-Pin_5) -> Net-(J7-Pin_4)
- R62 pad 2: /BMS/cell4 -> /BMS/cell9
- R63 pad 1: Net-(J1-Pin_6) -> Net-(J7-Pin_5)
- R63 pad 2: /BMS/cell5 -> /BMS/cell10
- R64 pad 1: Net-(J2-Pin_1) -> Net-(J7-Pin_6)
- R64 pad 2: /BMS/cell6 -> /BMS/cell11
- R65 pad 1: Net-(J2-Pin_2) -> Net-(J8-Pin_1)
- R65 pad 2: /BMS/cell7 -> /BMS/cell12
- R66 pad 1: Net-(J2-Pin_3) -> Net-(J8-Pin_2)
- R66 pad 2: /BMS/cell8 -> /BMS/cell13
- R67 pad 1: Net-(J2-Pin_4) -> Net-(J8-Pin_3)
- R67 pad 2: /BMS/cell9 -> /BMS/cell14
- R68 pad 1: Net-(J2-Pin_5) -> Net-(J8-Pin_4)
- R68 pad 2: /BMS/cell10 -> /BMS/cell15
- R69 pad 1: Net-(J2-Pin_6) -> Net-(J8-Pin_5)
- R69 pad 2: /BMS/cell11 -> GND2
- R70 pad 1: Net-(J3-Pin_1) -> Net-(J8-Pin_6)
- R70 pad 2: /BMS/cell12 -> /BMS/cell17
- R71 pad 1: Net-(J3-Pin_2) -> Net-(J9-Pin_1)
- R71 pad 2: /BMS/cell13 -> /BMS/cell18
- R72 pad 1: Net-(J3-Pin_3) -> Net-(J9-Pin_2)
- R72 pad 2: /BMS/cell14 -> /BMS/cell19
- R73 pad 1: Net-(J3-Pin_4) -> Net-(J9-Pin_3)
- R73 pad 2: /BMS/cell15 -> /BMS/cell20
- R74 pad 1: GND2 -> Net-(J9-Pin_4)
- R74 pad 2: /BMS/cell16 -> /BMS/cell21
- TP1 pad 1: /BMS/cell16 -> GND1
- TP1 pad 2: /BMS/cell17 -> /BMS/cell0
- TP10 pad 1: /BMS/cell25 -> /BMS/cell8
- TP10 pad 2: /BMS/cell26 -> /BMS/cell9
- TP11 pad 1: /BMS/cell26 -> /BMS/cell9
- TP11 pad 2: /BMS/cell27 -> /BMS/cell10
- TP12 pad 1: /BMS/cell27 -> /BMS/cell10
- TP12 pad 2: /BMS/cell28 -> /BMS/cell11
- TP13 pad 1: /BMS/cell28 -> /BMS/cell11
- TP13 pad 2: /BMS/cell29 -> /BMS/cell12
- TP14 pad 1: /BMS/cell29 -> /BMS/cell12
- TP14 pad 2: /BMS/cell30 -> /BMS/cell13
- TP15 pad 1: /BMS/cell30 -> /BMS/cell13
- TP15 pad 2: /BMS/cell31 -> /BMS/cell14
- TP16 pad 1: /BMS/cell0 -> /BMS/cell14
- TP16 pad 2: /BMS/cell1 -> /BMS/cell15
- TP17 pad 1: /BMS/cell1 -> /BMS/cell15
- TP17 pad 2: /BMS/cell2 -> GND2
- TP18 pad 1: /BMS/cell2 -> GND2
- TP18 pad 2: /BMS/cell3 -> /BMS/cell17
- TP19 pad 1: /BMS/cell3 -> /BMS/cell17
- TP19 pad 2: /BMS/cell4 -> /BMS/cell18
- TP2 pad 1: /BMS/cell17 -> /BMS/cell0
- TP2 pad 2: /BMS/cell18 -> /BMS/cell1
- TP20 pad 1: /BMS/cell4 -> /BMS/cell18
- TP20 pad 2: /BMS/cell5 -> /BMS/cell19
- TP21 pad 1: /BMS/cell5 -> /BMS/cell19
- TP21 pad 2: /BMS/cell6 -> /BMS/cell20
- TP22 pad 1: /BMS/cell6 -> /BMS/cell20
- TP22 pad 2: /BMS/cell7 -> /BMS/cell21
- TP23 pad 1: /BMS/cell7 -> /BMS/cell21
- TP23 pad 2: /BMS/cell8 -> /BMS/cell22
- TP24 pad 1: /BMS/cell8 -> /BMS/cell22
- TP24 pad 2: /BMS/cell9 -> /BMS/cell23
- TP25 pad 1: /BMS/cell9 -> /BMS/cell23
- TP25 pad 2: /BMS/cell10 -> /BMS/cell24
- TP26 pad 1: /BMS/cell10 -> /BMS/cell24
- TP26 pad 2: /BMS/cell11 -> /BMS/cell25
- TP27 pad 1: /BMS/cell11 -> /BMS/cell25
- TP27 pad 2: /BMS/cell12 -> /BMS/cell26
- TP28 pad 1: /BMS/cell12 -> /BMS/cell26
- TP28 pad 2: /BMS/cell13 -> /BMS/cell27
- TP29 pad 1: /BMS/cell13 -> /BMS/cell27
- TP29 pad 2: /BMS/cell14 -> /BMS/cell28
- TP3 pad 1: /BMS/cell18 -> /BMS/cell1
- TP3 pad 2: /BMS/cell19 -> /BMS/cell2
- TP30 pad 1: /BMS/cell14 -> /BMS/cell28
- TP30 pad 2: /BMS/cell15 -> /BMS/cell29
- TP31 pad 1: /BMS/cell15 -> /BMS/cell29
- TP31 pad 2: /BMS/cell16 -> /BMS/cell30
- TP32 pad 1: /BMS/cell31 -> /BMS/cell30
- TP32 pad 2: /BMS/cell32 -> /BMS/cell31
- TP4 pad 1: /BMS/cell19 -> /BMS/cell2
- TP4 pad 2: /BMS/cell20 -> /BMS/cell3
- TP5 pad 1: /BMS/cell20 -> /BMS/cell3
- TP5 pad 2: /BMS/cell21 -> /BMS/cell4
- TP6 pad 1: /BMS/cell21 -> /BMS/cell4
- TP6 pad 2: /BMS/cell22 -> /BMS/cell5
- TP7 pad 1: /BMS/cell22 -> /BMS/cell5
- TP7 pad 2: /BMS/cell23 -> /BMS/cell6
- TP8 pad 1: /BMS/cell23 -> /BMS/cell6
- TP8 pad 2: /BMS/cell24 -> /BMS/cell7
- TP9 pad 1: /BMS/cell24 -> /BMS/cell7
- TP9 pad 2: /BMS/cell25 -> /BMS/cell8
- U11 pad 4: /Temperature1/2V5_Ref -> +2V5
- U12 pad 1: Net-(R79-Pad2) -> VDDA
- U12 pad 3: GND -> VDDA
- U12 pad 4: /BMS/BMS2Reset -> unconnected-(U12-NC-Pad4)
- U2 pad 48: /BMS/cell16 -> GND2
- U5 pad 1: /BMS/cell30 -> /BMS/cell31
- U5 pad 16: /BMS/cell16 -> GND2
- U5 pad 2: /BMS/cell29 -> /BMS/cell30
- U5 pad 3: /BMS/cell28 -> /BMS/cell29
- U5 pad 4: /BMS/cell27 -> /BMS/cell28
- U5 pad 48: /BMS/cell31 -> /BMS/cell32
- U9 pad 4: /Temperature/2V5_Ref -> +2V5
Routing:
- net /BMS/cell4: track 0.00 -> 14.5 mm
- net /BMS/cell3: track 0.00 -> 13.8 mm
- net /BMS/cell0: track 0.00 -> 13.8 mm
- net /BMS/cell1: track 0.00 -> 13.7 mm
- net /BMS/cell2: track 0.00 -> 13.4 mm
- net /BMS/cell5: track 0.00 -> 12.6 mm
- net GND1: track 0.00 -> 9.63 mm
- net Net-(J6-Pin_1): track 0.00 -> 5.92 mm
- net Net-(J6-Pin_2): track 0.00 -> 5.62 mm
- net Net-(J6-Pin_6): track 0.00 -> 5.61 mm
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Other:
- board size 85 x 169.8 mm -> 85 x 128 mm

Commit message: Forgot to add footprints and values + updated PCB froms schematic
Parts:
- removed the C12 at (137.7, 171.7)
- removed the C13 at (137.7, 174.7)
- removed the C14 at (137.7, 177.7)
- removed the C20 at (82.0, 157.0)
- removed the C21 at (88.1, 157.0)
- removed the C22 at (90.4, 157.0)
- removed the C3 at (89.0, 144.7)
- removed the D2 at (42.5, 50.6)
- removed the D3 at (77.6, 63.9)
- removed U1: REF35250QDBVR, Package_SO:TSOP-6_1.65x3.05mm_P0.95mm
- removed the U10 at (85.1, 157.0)
- removed the U7 at (170.5, 188.9)
- added C61: 10uF, Capacitor_SMD:C_0805_2012Metric_Pad1.18x1.45mm_HandSolder, F.Cu at (-30.1, -2.12)
- added C62: 10uF, Capacitor_SMD:C_0805_2012Metric_Pad1.18x1.45mm_HandSolder, F.Cu at (-23.3, -2.12)
- added R89: 100k, Resistor_SMD:R_0805_2012Metric_Pad1.20x1.40mm_HandSolder, F.Cu at (-30.2, 0.86)
- added R90: 100k, Resistor_SMD:R_0805_2012Metric_Pad1.20x1.40mm_HandSolder, F.Cu at (-23.3, 0.86)
- added R91: 100k, Resistor_SMD:R_0805_2012Metric_Pad1.20x1.40mm_HandSolder, F.Cu at (-30.2, 3.81)
- added R94: 100k, Resistor_SMD:R_0805_2012Metric_Pad1.20x1.40mm_HandSolder, F.Cu at (-23.3, 3.81)
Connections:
- J2 pad 2: /I2C1_SCL -> /BMS/BMS1SCL
- J2 pad 3: /I2C1_SDA -> /BMS/BMS1SDA
- U11 pad 1: unconnected-(U11-GPIO2-Pad1) -> Net-(U11-GPIO2)
- U11 pad 2: unconnected-(U11-GPIO3-Pad2) -> Net-(U11-GPIO3)
- U9 pad 1: unconnected-(U9-GPIO2-Pad1) -> Net-(U9-GPIO2)
- U9 pad 2: unconnected-(U9-GPIO3-Pad2) -> Net-(U9-GPIO3)

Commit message: Use PeripheralSOM symbol
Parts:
- removed J1: SOMConnector, UTSVT_Connectors:Molex_53307-2071
- removed R2: 50, Resistor_SMD:R_0805_2012Metric
- added R92: 50, Resistor_SMD:R_0805_2012Metric, F.Cu at (-60.6, 66.5)
- added U1: ~, UTSVT_Special:PeripheralSOM, F.Cu at (190.1, 88.9)
